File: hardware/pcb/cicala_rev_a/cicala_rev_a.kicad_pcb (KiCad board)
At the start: 4 copper layers, 78 x 49 mm, 109 parts, among them J1 USB-C receptacle, J2 GDEY0213B74, J3 Protected LiPo + NTC, J4 TC2030 recovery pads, Q1 Si1308EDL, SW1 CATEGORY KSC321GLFS, SW2 NEXT KSC321GLFS, U1 ESP32-S3-WROOM-1-N16 / WROOM-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, U2 BQ25185DLH, U3 TPS63802DLA, U4 USBLC6-2SC6, U5 TPS22917DBVR, U6 TPS22917DBVR

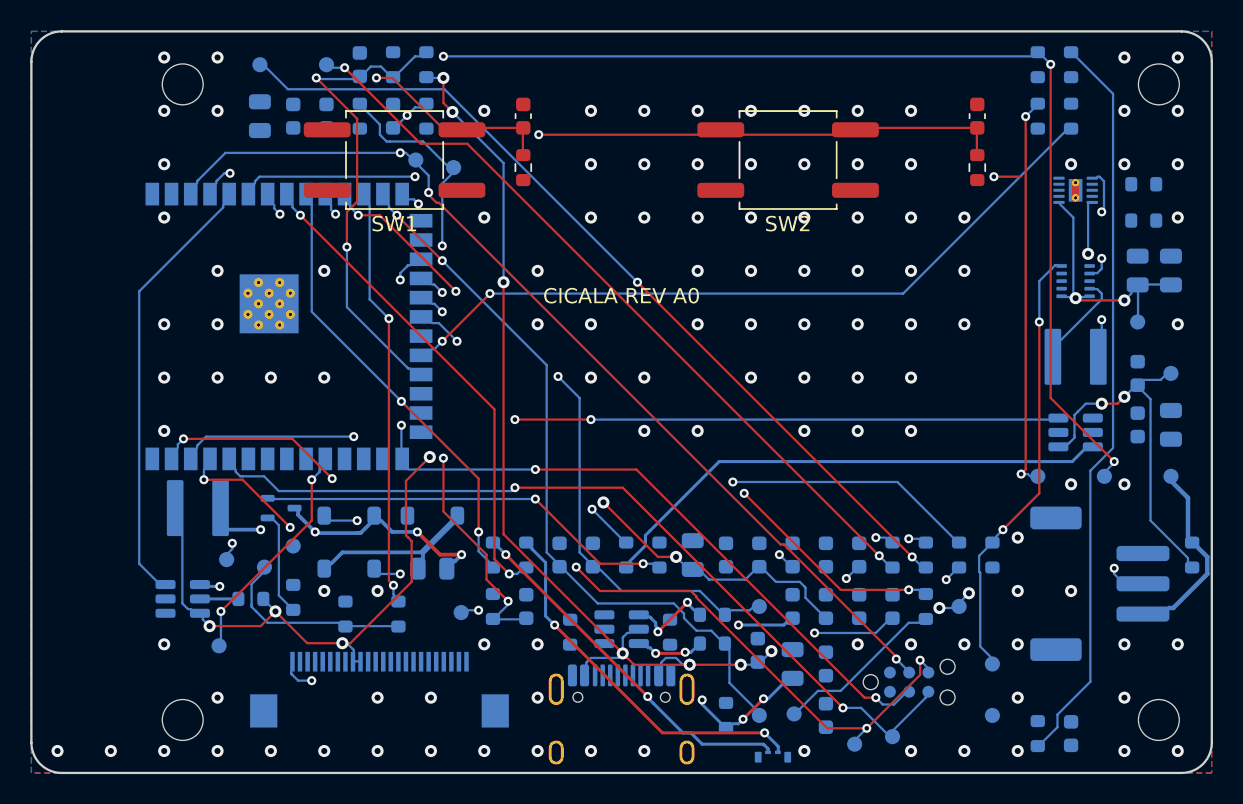
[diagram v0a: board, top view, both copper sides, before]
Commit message: fix(hw): connect rev A and add service silkscreen
Apply the checked fine-pitch escapes, coupled USB channel, placement refinements and native Cicala wordmark to the main board. Preserve the schematic, enclosure and documented mechanical reserves.

The board has 0 unconnected items and 0 schematic-parity errors. All remaining 58 DRC reports are retained copper islands; this is not a production release. Record power-layout, stitching, model and physical-validation risks in the PCB review.

Add continuous geometry audits and 21 PCB-tool regression tests. just test and hw-case-check pass; hw-pcb-check correctly fails before STEP export. No fabrication package was exported.
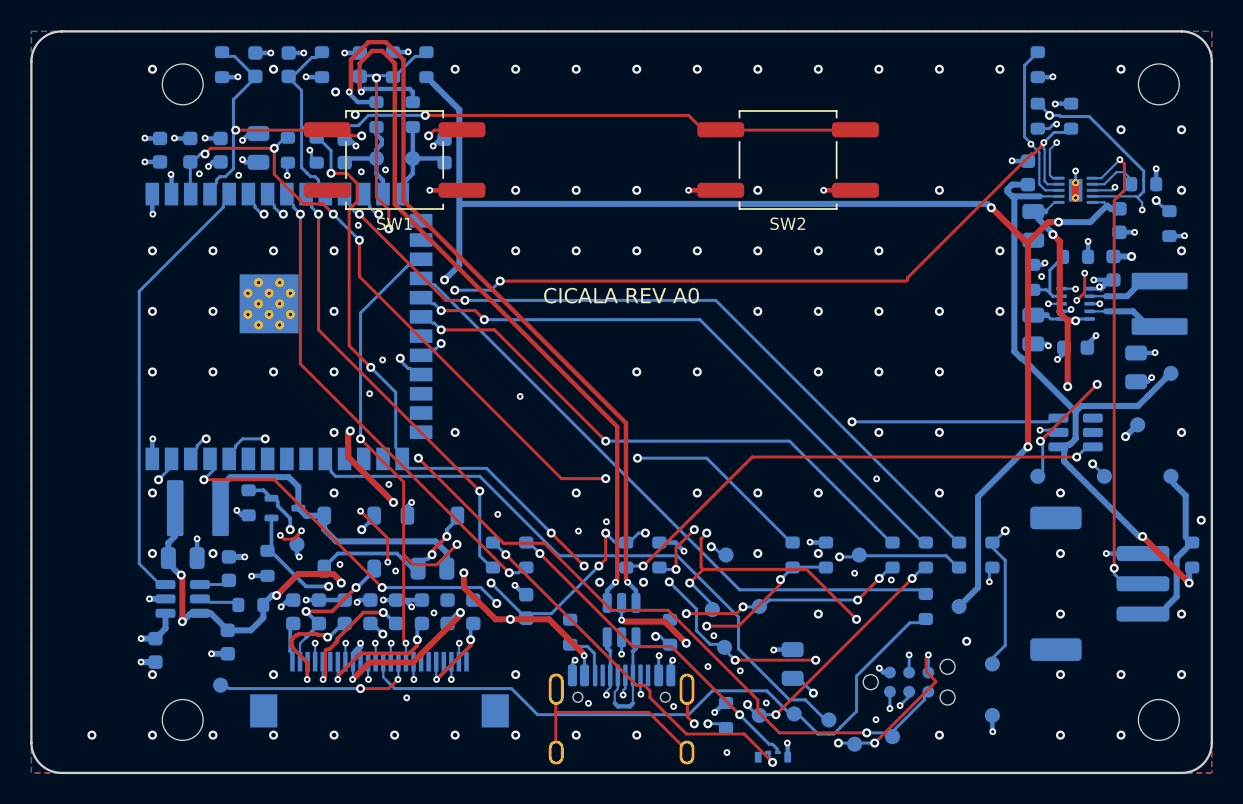
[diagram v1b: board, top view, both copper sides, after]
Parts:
- C25, C26, R21, R22: moved to B.Cu
- moved TP17 54.2 mm to (51.1, 48.7), turned to 0 degrees
- moved TP16 45.8 mm to (51.1, 41.5), turned to 0 degrees
- moved C26 45.6 mm to (20.0, 5.70)
- moved TP13 44.7 mm to (25.8, 11.9), turned to 0 degrees
- moved R22 43.8 mm to (22.2, 5.70)
- moved R3 41.4 mm to (25.8, 9.00), turned to -90 degrees
- moved TP6 40.6 mm to (55.7, 49.0)
- moved C24 39.6 mm to (20.3, 41.9)
- moved R4 38.5 mm to (28.2, 9.00), turned to -90 degrees
- moved C12 38.2 mm to (11.2, 44.4), turned to -90 degrees
- moved TP12 37.4 mm to (28.2, 11.9), turned to 0 degrees
- moved C14 37.3 mm to (16.1, 39.0)
- moved C4 37.1 mm to (74.9, 16.0), turned to -90 degrees
- moved TP1 36.4 mm to (48.8, 44.2), turned to 0 degrees
- moved C23 35.9 mm to (22.0, 41.9)
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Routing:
- net GND: track 0.00 -> 70.5 mm, vias 114 -> 182
- net Net-(R3-Pad1): track 3.35 -> 51.0 mm
- net Net-(R4-Pad1): track 4.74 -> 51.2 mm
- net Net-(U3-FB): track 48.0 -> 4.81 mm
- net EPD_VCOM: track 42.9 -> 1.53 mm, vias 2 -> 0
- net 3V3: track 0.00 -> 40.6 mm, vias 0 -> 26
- net Net-(U6-CT): track 41.6 -> 2.03 mm, vias 2 -> 0
- net USB_VBUS: track 102.5 -> 140.5 mm, vias 10 -> 12
- net USB_DN: track 44.8 -> 7.11 mm, vias 2 -> 0
- net USB_DP: track 39.5 -> 6.93 mm, vias 2 -> 0
- net PNL_CS: track 10.2 -> 42.6 mm
- net PNL_RESET: track 11.3 -> 43.0 mm, vias 0 -> 4
- net FACTORY_RESET_OD: track 13.9 -> 40.6 mm, vias 2 -> 0
- net EPD_BUSY: track 24.0 -> 50.7 mm, vias 2 -> 4
- net EPD_3V3: track 62.4 -> 36.3 mm, vias 6 -> 7
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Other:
- board text added: "+"
- board text added: "1:+ 2:NTC 3:-"
- board text added: "3V3"
- board text added: "4:BOOT 5:TX 6:RX"
- board text added: "BAT SENSE"
- board text added: "CELL AREA / NO COMPONENTS"
- board text added: "CHARGE"
- board text added: "J2 EPD"
- board text added: "J3 LiPo / NTC"
- board text added: "J4 1:3V3 2:GND 3:EN"
- board text added: "J4 RECOVERY"
- board text added: "NTC"
- board text added: "PROTECTED LiPo + NTC"
- board text added: "REV A0 / 4 LAYERS"
- board text added: "USB 5V"

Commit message: feat(hw): finalize Rev A prototype hardware and firmware
Complete the PCB and enclosure review, correct component ratings and footprints, add fitted 3D models, and export validated fabrication, assembly and print files.

Add Rev A firmware configuration, charger and power handling, USB flash/debug support, integration coverage, and build and manufacturing instructions.

Validation: zero configured ERC/DRC/parity findings; 45 PCB/export and 6 mesh tests; 14 nominal fit checks; 226 firmware cases passed with 3 platform skips; debug, charset and release/MCUboot builds; 84 Python and 101 website tests; strict docs build; prototype archive CRC/SHA256 verification. Physical prototype acceptance and factory CAM review remain pending.
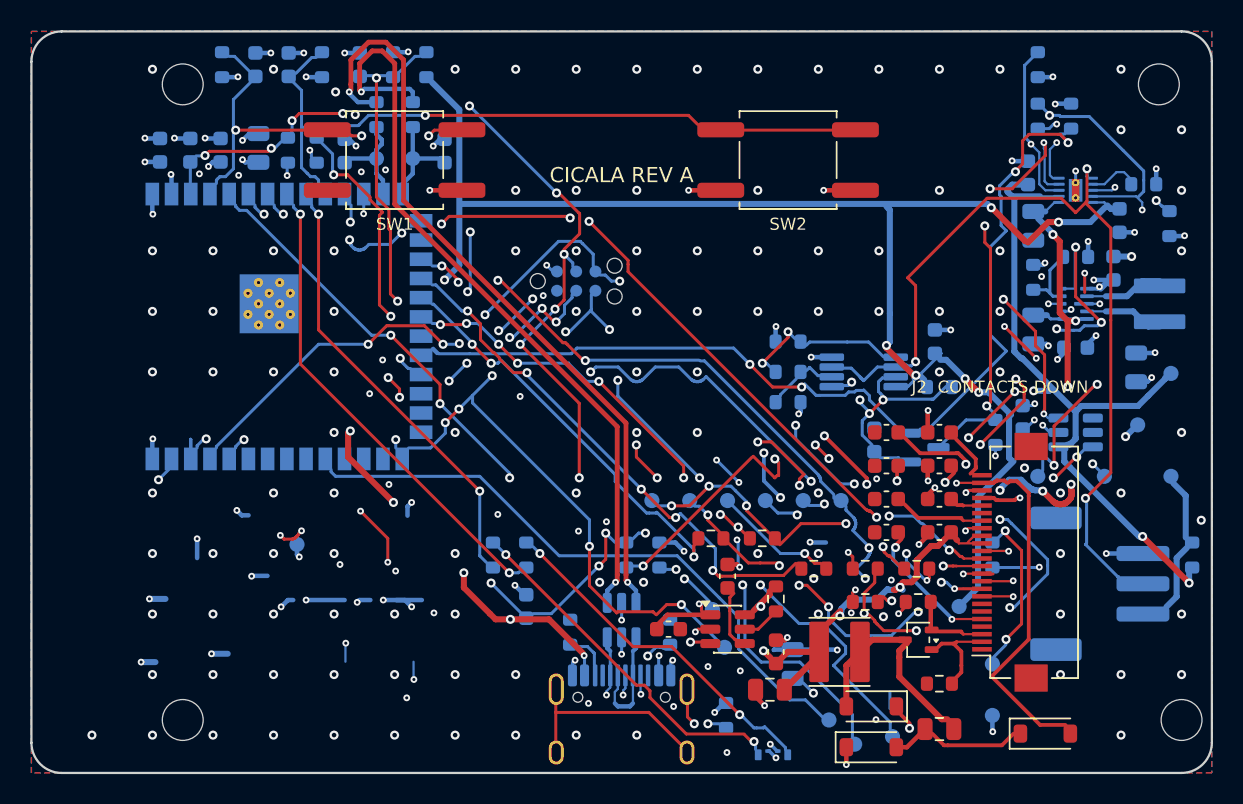
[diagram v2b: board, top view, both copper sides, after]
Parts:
- added C32: 100nF, Capacitor_SMD:C_0603_1608Metric, B.Cu at (62.7, 24.0)
- added C33: 100nF, Capacitor_SMD:C_0603_1608Metric, B.Cu at (58.7, 30.5)
- added C34: 10uF 10V, Capacitor_SMD:C_0603_1608Metric, B.Cu at (68.5, 29.0)
- added Q2: 2N7002P, Package_TO_SOT_SMD:SOT-23, B.Cu at (62.0, 31.0)
- added R35: 820k, Resistor_SMD:R_0603_1608Metric, B.Cu at (53.0, 24.0)
- added R36: 210k, Resistor_SMD:R_0603_1608Metric, B.Cu at (53.0, 26.0)
- added R37: 82.5k, Resistor_SMD:R_0603_1608Metric, B.Cu at (53.0, 28.0)
- added R38: 100k, Resistor_SMD:R_0603_1608Metric, B.Cu at (63.0, 27.0)
- added R39: 100k, Resistor_SMD:R_0603_1608Metric, B.Cu at (66.7, 30.0)
- added U7: TLV9022DGK, Package_SO:VSSOP-8_3x3mm_P0.65mm, B.Cu at (58.0, 26.0)
- C10: value 47uF 6.3V -> 47uF 10V
- C12, C13, C14, C15, C16, C17, C18, C19, C20, C21, C22, C23, C24, D1, D2, D3, J2, L1, Q1, R18, R19, R20, R27, R28, R29, R30, R31, R32, U6: moved to F.Cu
- C30: value 47uF -> 47uF 10V
- C31: value 1nF 2kV -> 1nF 2kV DNP
- C4: value 1uF 25V -> 10uF 10V
- C6: value 1uF 16V -> 10uF 10V
- C8: value 10uF 25V -> 47uF 10V
- R13: value 100k -> 4.7k
- R21, R22: value 47k -> 22k
- SW1: value CATEGORY KSC321GLFS -> CATEGORY KSC323GLFG
- SW2: value NEXT KSC321GLFS -> NEXT KSC323GLFG
- U1: value ESP32-S3-WROOM-1-N16 / WROOM-1U-N16 -> ESP32-S3-WROOM-1-N16
- moved D1 47.3 mm to (70.0, 49.9)
- moved R19 45.1 mm to (63.0, 46.6), turned to 180 degrees
- moved R20 44.7 mm to (61.6, 41.2), turned to 180 degrees
- moved C24 44.3 mm to (63.0, 30.0), turned to 180 degrees
- moved L1 43.5 mm to (56.4, 44.5)
- moved Q1 42.7 mm to (61.6, 43.7), turned to 180 degrees
- moved J2 42.5 mm to (67.7, 38.6), turned to 90 degrees
- moved C22 40.5 mm to (63.0, 32.2), turned to 180 degrees
- moved TP20 40.4 mm to (54.0, 34.5), turned to 0 degrees
- moved C15 39.8 mm to (51.8, 47.0), turned to 180 degrees
- moved C23 39.3 mm to (59.5, 30.0), turned to 180 degrees
- moved D3 36.7 mm to (58.5, 48.1)
- moved C21 36.7 mm to (63.0, 34.4), turned to 180 degrees
- moved C13 36.2 mm to (52.2, 44.5), turned to 90 degrees
- moved U6 36.1 mm to (49.0, 43.0)
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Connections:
- U2 pad 4: CHG_ENABLE -> CHG_CE
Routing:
- net EPD_VGH: track 18.0 -> 57.2 mm, vias 3 -> 9
- net CHG_CE: track 0.00 -> 29.0 mm, vias 0 -> 4
- net VBAT_SENSE_EN: track 58.7 -> 83.5 mm, vias 2 -> 4
- net BATT_NTC: track 30.2 -> 54.6 mm, vias 2 -> 3
- net GND: track 70.5 -> 93.3 mm, vias 182 -> 208
- net EPD_VGL: track 8.23 -> 30.3 mm
- net 3V3: track 40.6 -> 61.5 mm, vias 26 -> 30
- net EPD_RESE: track 24.3 -> 4.87 mm, vias 2 -> 0
- net EPD_PWR_EN: track 27.6 -> 46.7 mm, vias 0 -> 4
- net REG_PG: track 27.1 -> 45.4 mm, vias 2 -> 7
- net UART0_RX: track 54.8 -> 70.9 mm, vias 3 -> 10
- net EPD_GDR: track 20.8 -> 5.85 mm, vias 2 -> 0
- net PNL_RESET: track 43.0 -> 28.2 mm, vias 4 -> 5
- net PNL_MOSI: track 42.0 -> 27.7 mm, vias 4 -> 6
- net /Charge temperature guard/TEMP_OK: track 0.00 -> 14.3 mm, vias 0 -> 4
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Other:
- board text added: "CICALA REV A"
- board text added: "J2 CONTACTS DOWN"
- board text added: "REV A / 4 LAYERS"
- board text removed: "BAT SENSE"
- board text removed: "CELL AREA / NO COMPONENTS"
- board text removed: "CICALA REV A0"
- board text removed: "J2 EPD"
- board text removed: "REV A0 / 4 LAYERS"
